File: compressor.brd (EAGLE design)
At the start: 100 x 80 mm, 41 parts, among them U1 MAX5419LETA+, U2 MAX5419LETA+

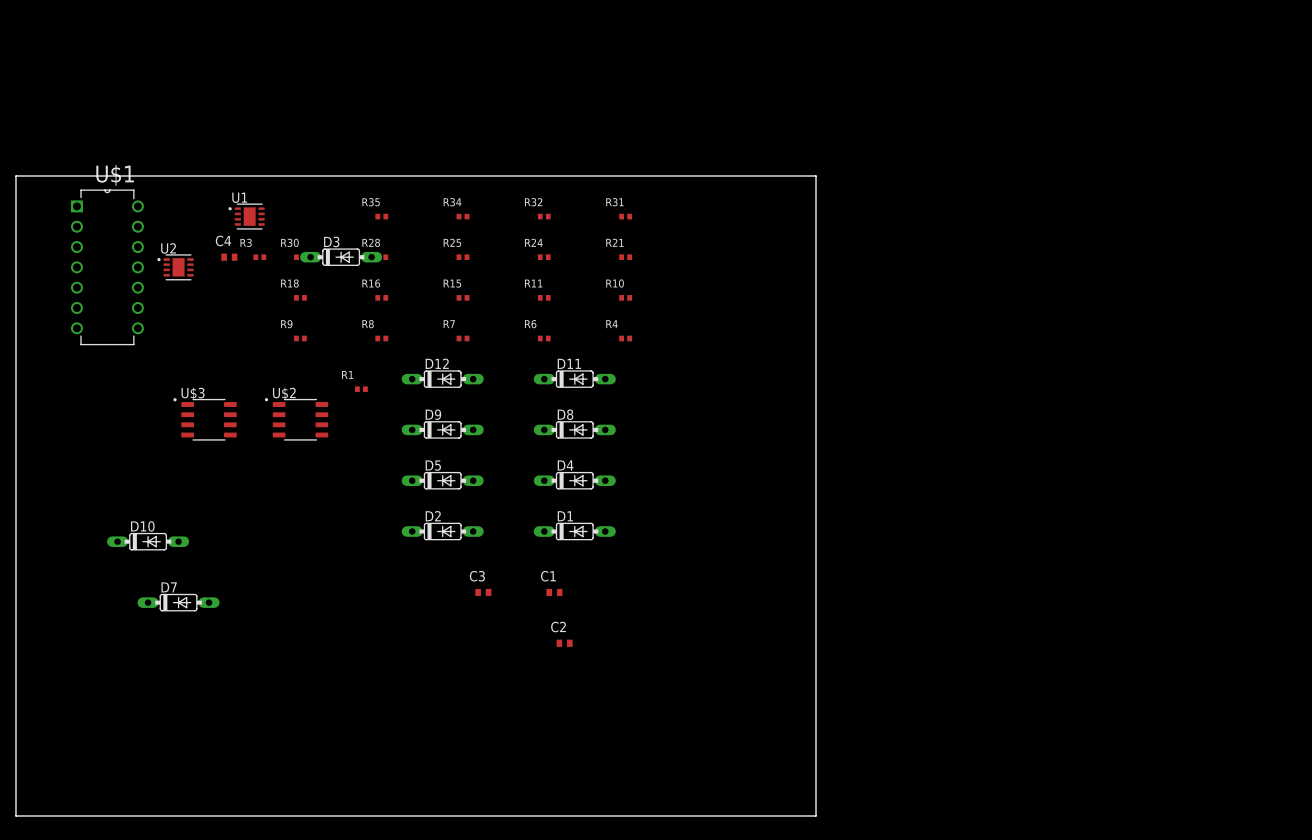
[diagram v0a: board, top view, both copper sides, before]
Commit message: rm cache files, add boards for components
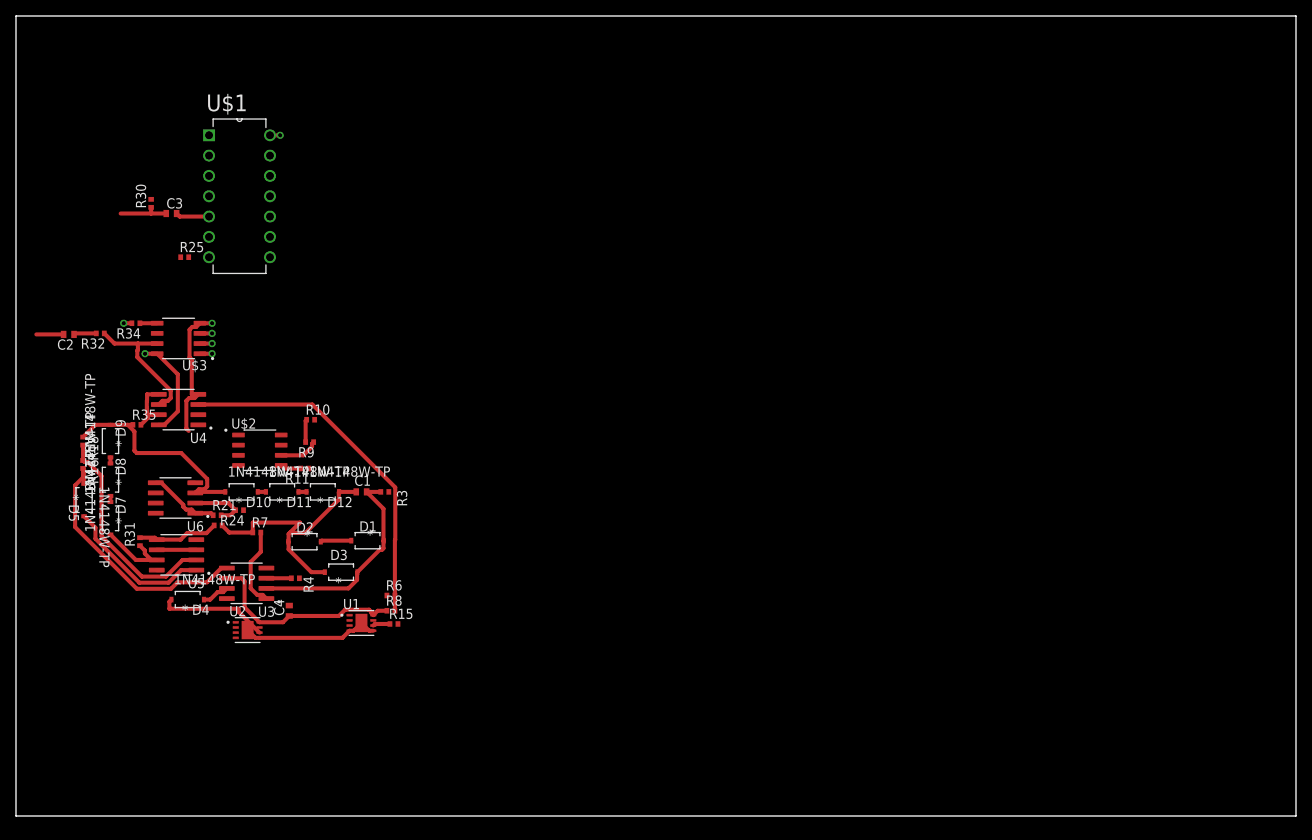
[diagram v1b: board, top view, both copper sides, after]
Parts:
- removed R1: 0, rcl:R0402
- added U3, U4, U5, U6: LM4562MAX/NOPB, LM4562MAX_NOPB:SOIC127P599X175-8N
- D1, D10, D11, D12, D2, D3, D4, D5, D7, D8, D9: value 1N4148DO35-7 -> 1N4148W-TP; device diode:DO35-7 -> 1N4148W-TP:SOD123
- moved R31 73.1 mm to (15.5, 34.3), turned to 90 degrees
- moved C2 73.0 mm to (6.60, 60.2), turned to 180 degrees
- moved C3 61.4 mm to (19.4, 75.3)
- moved R21 60.4 mm to (25.1, 37.6)
- moved D8 58.4 mm to (11.8, 42.0), turned to 90 degrees
- moved R32 57.4 mm to (10.5, 60.3), turned to 180 degrees
- moved U1 52.7 mm to (43.2, 24.1)
- moved R4 51.0 mm to (34.9, 29.7), turned to 180 degrees
- moved D4 50.6 mm to (21.5, 27.1)
- moved R24 49.5 mm to (27.9, 38.2), turned to 180 degrees
- moved U2 46.2 mm to (29.0, 23.2)
- moved D5 44.9 mm to (8.51, 39.5), turned to 270 degrees
- moved C4 44.8 mm to (34.2, 25.7), turned to 90 degrees
- moved R34 43.0 mm to (15.0, 61.6), turned to 180 degrees
- moved R16 42.8 mm to (8.38, 43.9), turned to 270 degrees
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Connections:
- removed net N$22: R28.1, R31.2
- removed net N$23: D7.C, R31.1
- removed net N$33: D5.A
- new net N$2: D7.C, R31.1, U5.7
- new net N$4: D5.A, U5.1
- new net N$8: R28.1, R31.2, U5.5
- net H_0: now also U3.6
- net N$1: now also U3.1
- net N$14: now also U3.7
- net N$15: now also U3.5
- net N$16: now also U5.2
- net N$18: now also U6.1, U6.5
- net N$19: now also U6.2
- net N$26: now also U6.3
- net N$27: now also U4.5, U4.7
- net N$3: now also U3.2
- net N$6: now also U4.3
- net N$7: now also U4.2
- net P0B_0: no longer R1.2
- net P0B_1: now also U4.6
- net PA0: now also U4.1
- net PA1: now also U6.6
- net PB0: now also U3.3
- net PB1: now also U6.7
- net VDD: now also U3.8, U4.8, U5.8, U6.8
- net VREF: now also U5.3, U5.6; no longer R1.1
- net VSS: now also U3.4, U4.4, U5.4, U6.4
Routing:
- net N$6: track 0.00 -> 44.3 mm
- net VSS: track 0.00 -> 35.9 mm, vias 0 -> 1
- net N$15: track 0.00 -> 32.9 mm
- net N$21: track 0.00 -> 32.0 mm
- net N$26: track 0.00 -> 27.6 mm
- net N$16: track 0.00 -> 27.4 mm
- net N$3: track 0.00 -> 27.0 mm
- net H_0: track 0.00 -> 25.4 mm
- net N$4: track 0.00 -> 18.9 mm
- net P0B_1: track 0.00 -> 17.5 mm
- net VDD: track 0.00 -> 14.8 mm, vias 0 -> 2
- net L_1: track 0.00 -> 14.0 mm
- net N$2: track 0.00 -> 10.2 mm
- net N$8: track 0.00 -> 10.1 mm
- net N$1: track 0.00 -> 9.99 mm
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- added copper zone on layer 2, net VSS
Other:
- board size 100 x 80 mm -> 160 x 100 mm

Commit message: finish compressor routing, and sloppy combined routing
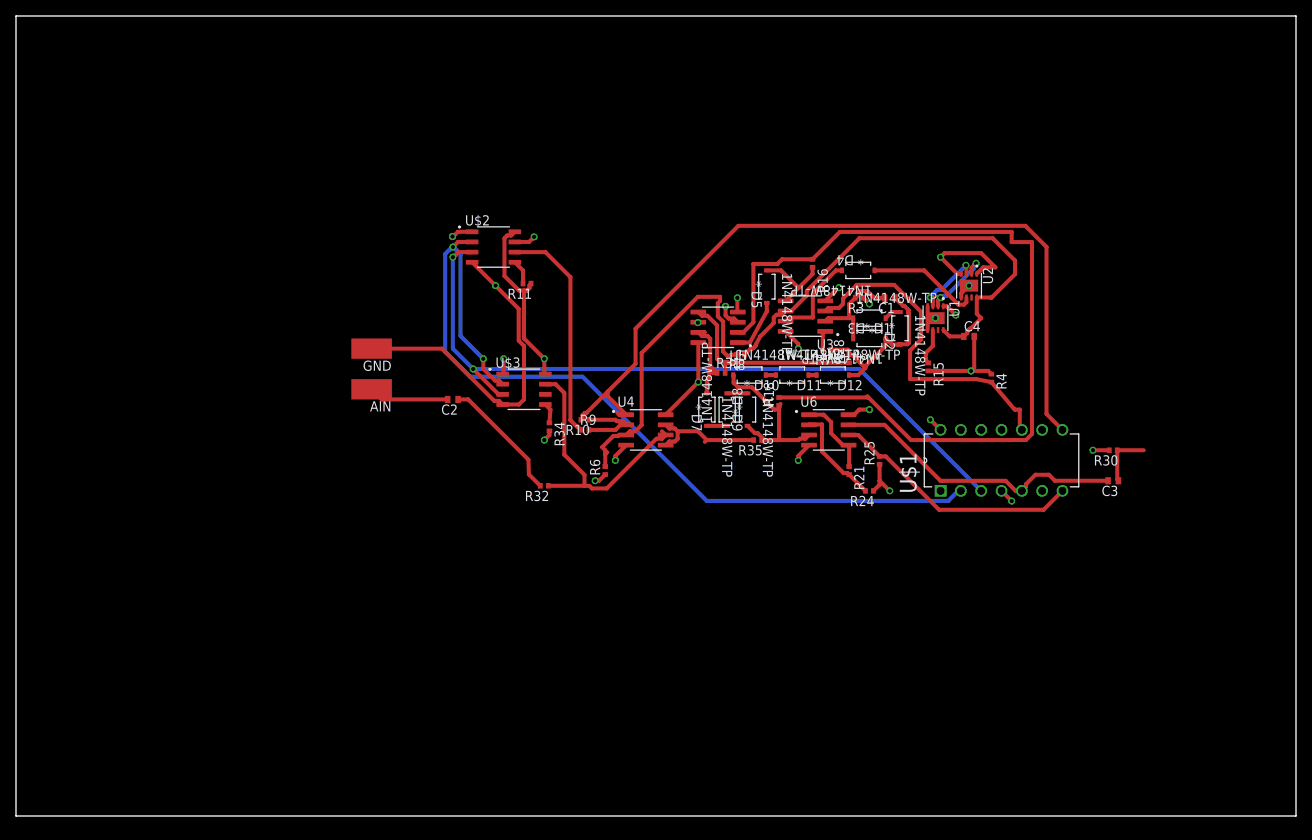
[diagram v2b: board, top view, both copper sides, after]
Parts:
- added AIN, GND: (no value), wirepad:SMD2,54-5,08
- moved R30 124.2 mm to (137.2, 45.7), turned to 180 degrees
- moved C3 122.4 mm to (137.2, 41.9), turned to 180 degrees
- moved U$1 101.4 mm to (130.8, 48.3), turned to 90 degrees
- moved U2 99.9 mm to (119.1, 66.3), turned to 270 degrees
- moved R16 94.6 mm to (99.6, 69.1)
- moved D4 93.4 mm to (105.3, 68.2), turned to 180 degrees
- moved C4 91.6 mm to (119.1, 59.9), turned to 0 degrees
- moved R4 90.5 mm to (121.9, 54.7), turned to 270 degrees
- moved R25 90.5 mm to (108.0, 44.5), turned to 90 degrees
- moved D5 89.4 mm to (93.9, 66.2)
- moved R18 87.1 mm to (95.4, 51.8), turned to 90 degrees
- moved U6 82.1 mm to (101.6, 48.3), turned to 0 degrees
- moved R28 81.6 mm to (104.1, 57.1), turned to 90 degrees
- moved U1 81.2 mm to (114.9, 62.2), turned to 270 degrees
- moved D9 79.7 mm to (91.4, 50.8), turned to 270 degrees
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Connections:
- removed net P0B_0: U$2.7
- net AIN: now also AIN.1
- net VREF: now also U$2.7
- net VSS: now also GND.1
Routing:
- net VSS: track 35.9 -> 225.5 mm, vias 1 -> 9
- net VREF: track 5.96 -> 172.1 mm, vias 1 -> 8
- net VDD: track 14.8 -> 133.6 mm, vias 2 -> 7
- net SCK: track 1.52 -> 109.0 mm, vias 1 -> 2
- net PA0: track 0.00 -> 100.8 mm
- net SDI/O: track 1.52 -> 92.5 mm, vias 1 -> 2
- net N$16: track 27.4 -> 105.8 mm
- net PB0: track 3.13 -> 42.1 mm
- net H_0: track 25.4 -> 58.7 mm
- net PB1: track 4.21 -> 37.2 mm
- net PA1: track 0.00 -> 31.6 mm
- net P0W_0: track 4.95 -> 27.9 mm
- net N$15: track 32.9 -> 10.5 mm
- net P0B_1: track 17.5 -> 33.7 mm
- net N$8: track 10.1 -> 25.4 mm
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- removed copper zone on layer 2, net VSS

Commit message: corrections
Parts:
- removed R30: 1M, rcl:R0402
- C2: value 0.1 -> 0.1u
- moved C1 84.7 mm to (40.4, 15.4), turned to 90 degrees
- moved R28 83.4 mm to (33.7, 12.6), turned to 0 degrees
- moved D12 81.9 mm to (34.0, 9.53), turned to 90 degrees
- moved R3 80.2 mm to (42.0, 15.6), turned to 90 degrees
- moved R16 79.4 mm to (36.2, 21.2), turned to 0 degrees
- moved D11 79.4 mm to (31.8, 9.91), turned to 270 degrees
- moved C3 77.4 mm to (66.7, 9.91), turned to 270 degrees
- moved D10 76.9 mm to (29.5, 9.91), turned to 90 degrees
- moved D7 76.7 mm to (21.0, 10.8)
- moved D8 76.5 mm to (23.9, 10.4)
- moved R35 76.3 mm to (27.3, 7.62)
- moved D9 76.2 mm to (26.5, 10.8)
- moved U$1 75.1 mm to (63.8, 14.5)
- moved U2 74.6 mm to (58.3, 23.1)
- moved D5 73.8 mm to (37.7, 18.3)
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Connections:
- net AOUT: no longer R30.1
- net VSS: no longer R30.2
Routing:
- net VSS: track 225.5 -> 130.6 mm, vias 9 -> 7
- net SCK: track 109.0 -> 53.6 mm
- net PA0: track 100.8 -> 72.5 mm
- net SDI/O: track 92.5 -> 65.0 mm
- net P0W_0: track 27.9 -> 2.34 mm
- net VREF: track 172.1 -> 147.2 mm
- net PB0: track 42.1 -> 20.1 mm
- net N$16: track 105.8 -> 84.2 mm
- net N$8: track 25.4 -> 9.03 mm
- net VDD: track 133.6 -> 118.8 mm
- net P0B_1: track 33.7 -> 19.2 mm
- net N$6: track 39.9 -> 25.9 mm
- net N$30: track 15.8 -> 4.87 mm
- net N$27: track 14.9 -> 24.6 mm
- net PB1: track 37.2 -> 28.2 mm
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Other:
- board outline removed

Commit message: updates
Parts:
- removed C3: 1.5u, rcl:C0402
- removed R15: 100k, rcl:R0402
- removed R4: 10k, rcl:R0402
- added R1: 100k, rcl:R0402
- C2: value 0.1u -> 10u
- moved R18 1.27 mm to (35.9, 11.3)
- moved R21 1.02 mm to (42.2, 5.97)
- renumbered AIN to IN_COMP, U$1 to 100POT1_COMP, U$2 to 10POT1_COMP, U$3 to 10POT2_COMP, U1 to 200POT2_COMP, U2 to 200POT1_COMP, U3 to OPAMP1_COMP, U4 to OPAMP2_COMP, U5 to OPAMP3_COMP, U6 to OPAMP4_COMP
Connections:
- net AIN renamed IN_COMP
- net CS0 renamed CS0_COMP
- net CS1 renamed CS1_COMP
- net CS2 renamed CS2_COMP
- net H_0 renamed H1_COMP
- net N$1 renamed OUT_A1_COMP
- net N$14 renamed OUT_B1_COMP
- net N$15 renamed POS_B1_COMP
- net N$16 renamed NEG_A3_COMP
- net N$19 renamed NEG_A4_COMP
- net N$2 renamed OUT_B3_COMP
- net N$3 renamed NEG_A1_COMP
- net N$4 renamed OUT_A3_COMP
- net N$6 renamed POS_A2_COMP
- net N$7 renamed NEG_A2_COMP
- net P0A_0 renamed P0A1_COMP
- net P0A_1 renamed P0A2_COMP
- net P0W_0 renamed P0W1_COMP
- net SCL renamed SCL_COMP
- net SDA renamed SDA_COMP
- net VSS renamed GND
- removed net AOUT: C3.1
- removed net L_0: 200POT2_COMP.6, R15.1
- removed net L_1: 200POT1_COMP.6, D4.C
- removed net N$18: OPAMP4_COMP.1, OPAMP4_COMP.5, R21.1
- removed net N$26: D10.C, D9.A, OPAMP4_COMP.3, R18.1, R35.1
- removed net N$27: OPAMP2_COMP.5, OPAMP2_COMP.7, R35.2
- removed net N$8: OPAMP3_COMP.5, R28.1, R31.2
- removed net P0B_1: 10POT2_COMP.7, OPAMP2_COMP.6, R32.1
- removed net PA0: 100POT1_COMP.8, OPAMP2_COMP.1, R10.2
- removed net PA1: 100POT1_COMP.7, OPAMP4_COMP.6, R25.2
- removed net PB0: 100POT1_COMP.10, OPAMP1_COMP.3, R4.2
- removed net PB1: 100POT1_COMP.5, C3.2, OPAMP4_COMP.7
- removed net RS: 100POT1_COMP.11
- removed net SHDN: 100POT1_COMP.12
- new net L1_COMP: 200POT1_COMP.6, 200POT1_COMP.7, D4.C
- new net L2_COMP: 200POT2_COMP.6, 200POT2_COMP.7, R1.2
- new net NEG_B2_COMP: OPAMP2_COMP.6, OPAMP2_COMP.7, R35.2
- new net NEG_B3_COMP: OPAMP3_COMP.6, R28.1, R31.2
- new net NEG_B4_COMP: 100POT1_COMP.5, OPAMP4_COMP.6, R25.2
- new net OUT_A2_COMP: 100POT1_COMP.10, OPAMP2_COMP.1, R10.2
- new net OUT_A4_COMP: OPAMP4_COMP.1, OPAMP4_COMP.5, R18.1, R21.1
- new net OUT_COMP: 100POT1_COMP.6, 100POT1_COMP.7, OPAMP4_COMP.7
- new net POS_A1_COMP: 100POT1_COMP.9, OPAMP1_COMP.3
- new net POS_A4_COMP: D10.C, D9.A, OPAMP4_COMP.3, R35.1
- new net POS_B2_COMP: 10POT2_COMP.6, 10POT2_COMP.7, OPAMP2_COMP.5, R32.1
- net VDD: no longer 100POT1_COMP.14, 10POT1_COMP.8, 10POT2_COMP.8, 200POT1_COMP.1, 200POT1_COMP.4, 200POT2_COMP.1
- net VREF: now also 100POT1_COMP.11, 100POT1_COMP.12, 100POT1_COMP.14, 100POT1_COMP.8, 10POT1_COMP.8, 10POT2_COMP.8, 200POT1_COMP.1, 200POT1_COMP.4, 200POT2_COMP.1, OPAMP3_COMP.5, R1.1; no longer OPAMP3_COMP.6, R15.2, R4.1
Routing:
- net OUT_A2_COMP: track 0.00 -> 78.7 mm
- net PA0: track 72.5 -> 0.00 mm
- net VDD: track 118.8 -> 51.7 mm, vias 7 -> 4
- net OUT_COMP: track 0.00 -> 29.7 mm
- net PB1: track 28.2 -> 0.00 mm
- net NEG_B2_COMP: track 0.00 -> 26.0 mm
- net PA1: track 25.1 -> 0.00 mm
- net N$27: track 24.6 -> 0.00 mm
- net VREF: track 147.2 -> 170.3 mm, vias 8 -> 10
- net POS_A1_COMP: track 0.00 -> 20.6 mm
- net PB0: track 20.1 -> 0.00 mm
- net POS_B2_COMP: track 0.00 -> 19.4 mm
- net P0B_1: track 19.2 -> 0.00 mm
- net NEG_B4_COMP: track 0.00 -> 17.4 mm
- net N$26: track 16.3 -> 0.00 mm
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
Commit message: v2 of board finished
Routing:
- net VREF: track 170.3 -> 166.8 mm
- net OUT_B3_COMP: track 15.6 -> 14.8 mm
- net OUT_COMP: track 29.7 -> 29.0 mm
- net NEG_A3_COMP: track 86.9 -> 86.2 mm
